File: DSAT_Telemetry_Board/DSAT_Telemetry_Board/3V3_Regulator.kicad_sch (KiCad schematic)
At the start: 5 parts

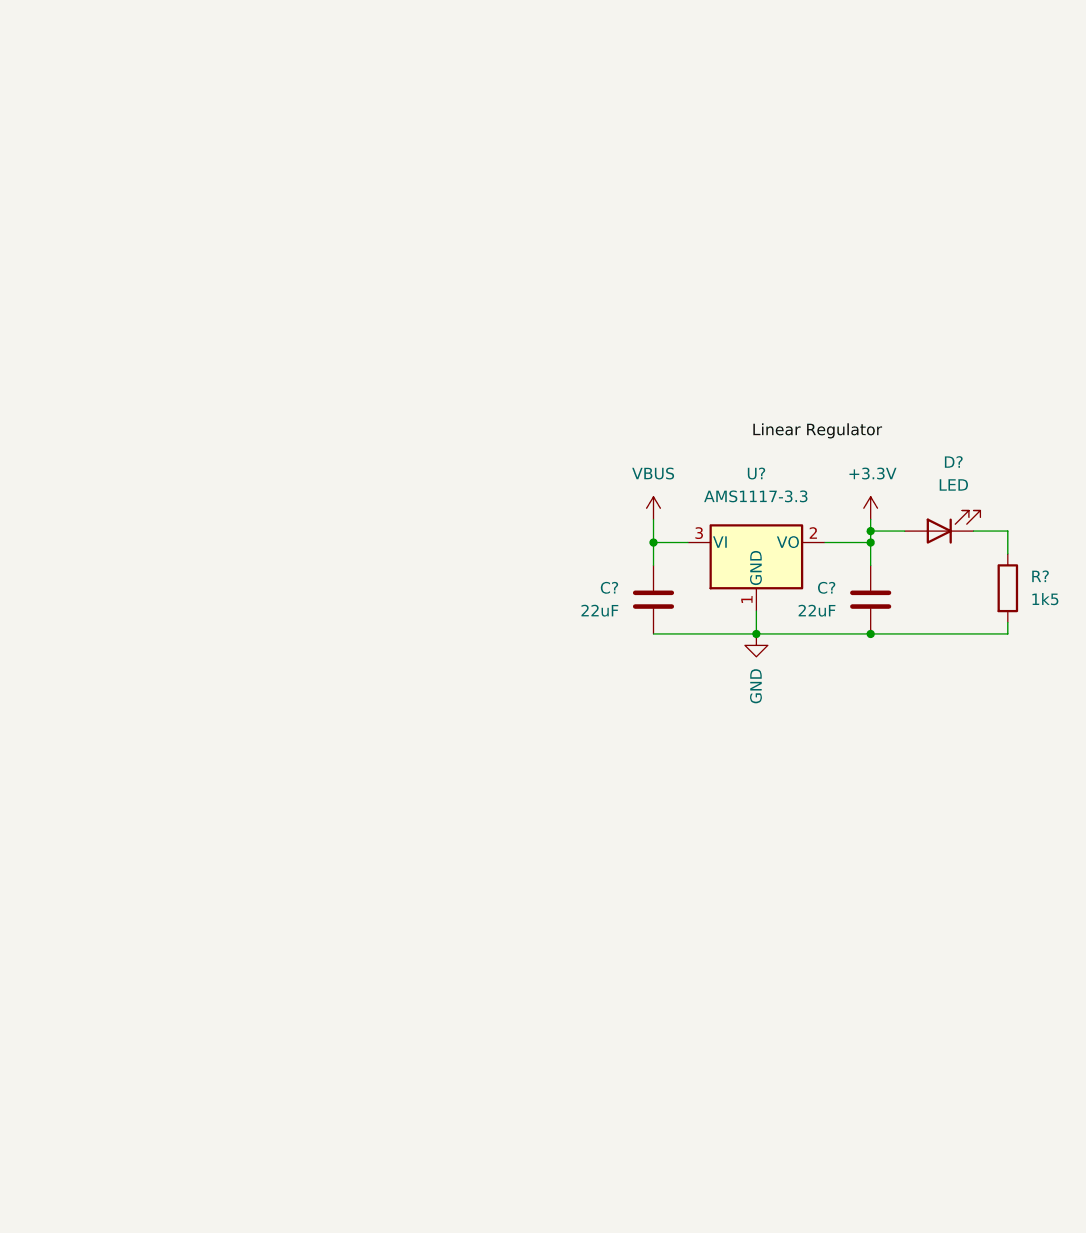
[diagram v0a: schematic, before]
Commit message: Added Matching Networks/Linear Regulator/Watchdog Pins
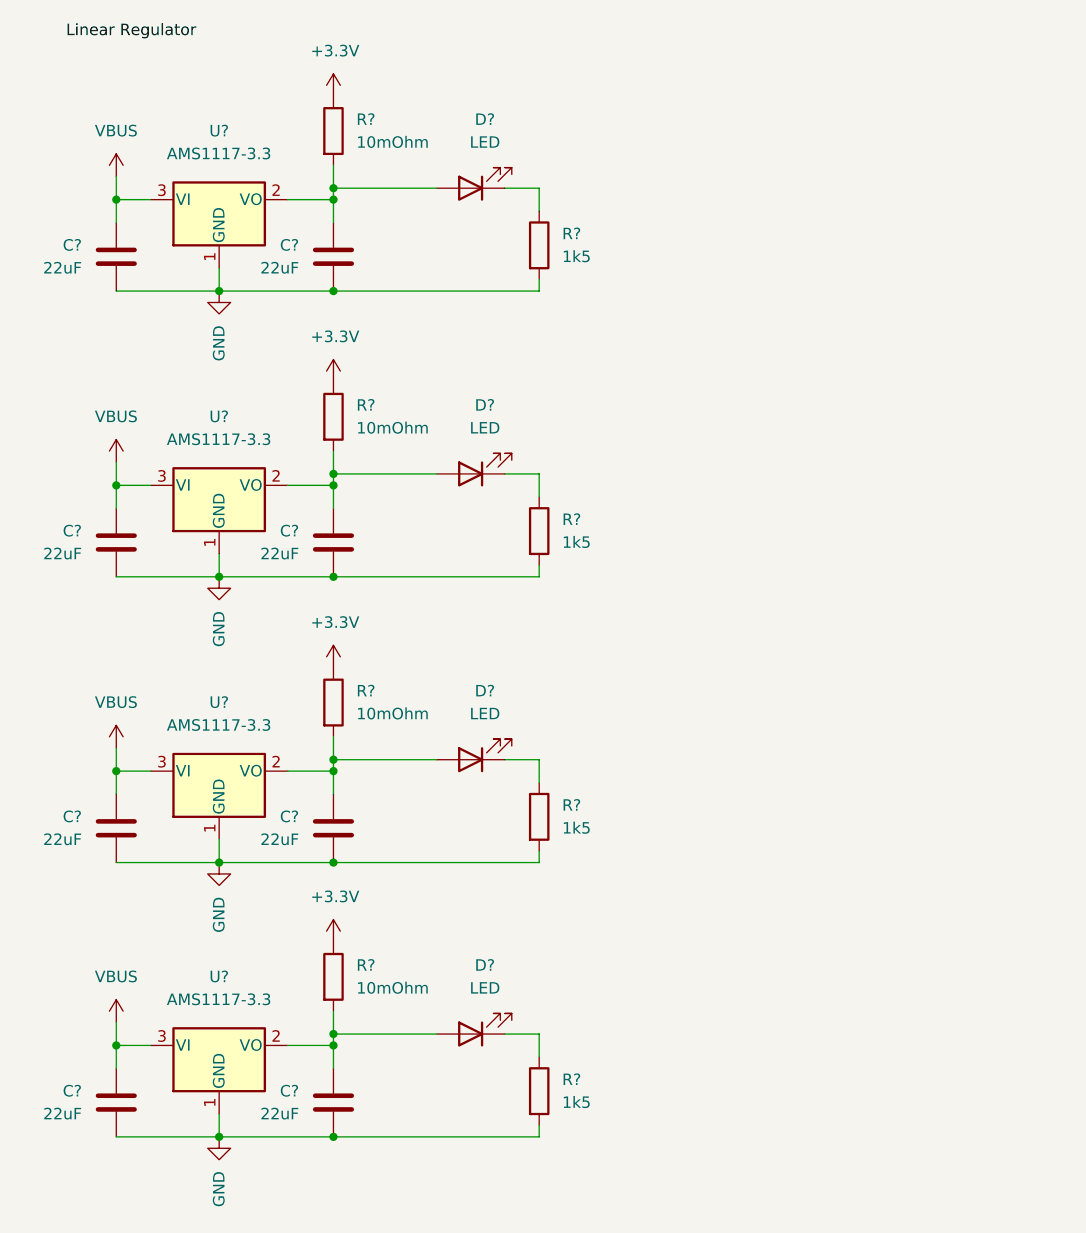
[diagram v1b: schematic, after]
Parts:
- added C? (x6): 22uF, symbol Device:C
- added D? (x3): LED, symbol Device:LED
- added R? (x3): 1k5, symbol Device:R
- added R? (x4): 10mOhm, symbol Device:R
- added U? (x3): AMS1117-3.3, Package_TO_SOT_SMD:SOT-223-3_TabPin2, symbol Regulator_Linear:AMS1117-3.3
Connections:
- net +3.3V: now also R?.1, R?.1, R?.1, R?.1; no longer C?.2, D?.2 (A), U?.2 (VO)
- net GND: now also C?.1, C?.1, C?.1, C?.1, C?.1, C?.1, R?.2, R?.2, R?.2, U?.1 (GND), U?.1 (GND), U?.1 (GND)
- net VBUS: now also C?.2, C?.2, C?.2, U?.3 (VI), U?.3 (VI), U?.3 (VI)
- new net: C?.2, D?.2 (A), R?.2, U?.2 (VO) (x4)
- new net: D?.1 (K), R?.1 (x3)
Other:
- moved on the sheet: C?, D?, R?, U?
